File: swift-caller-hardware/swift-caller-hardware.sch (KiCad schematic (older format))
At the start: 3 parts

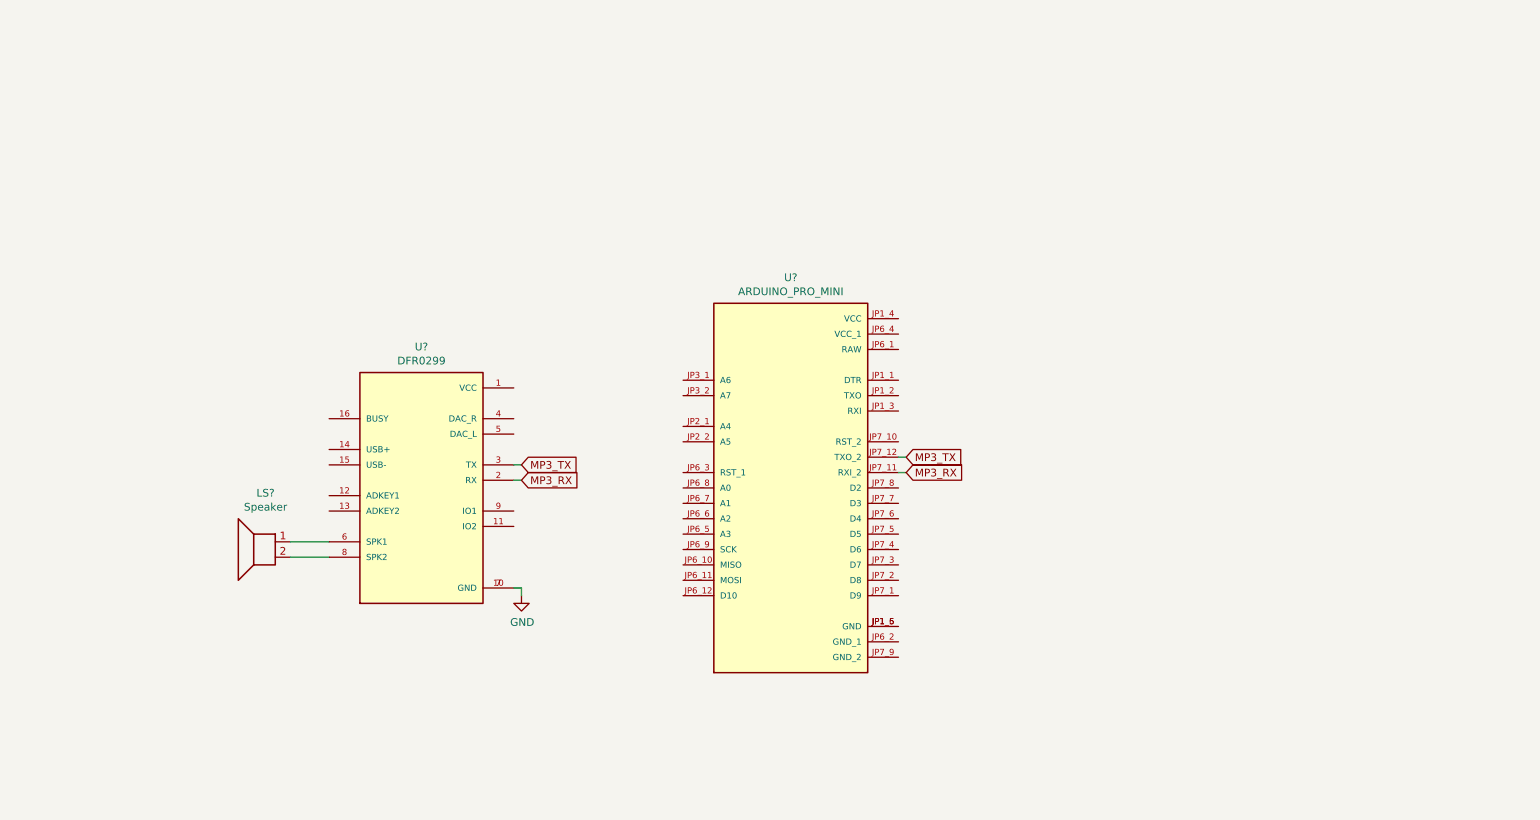
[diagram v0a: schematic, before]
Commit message: Update schematic and rename sub-directories
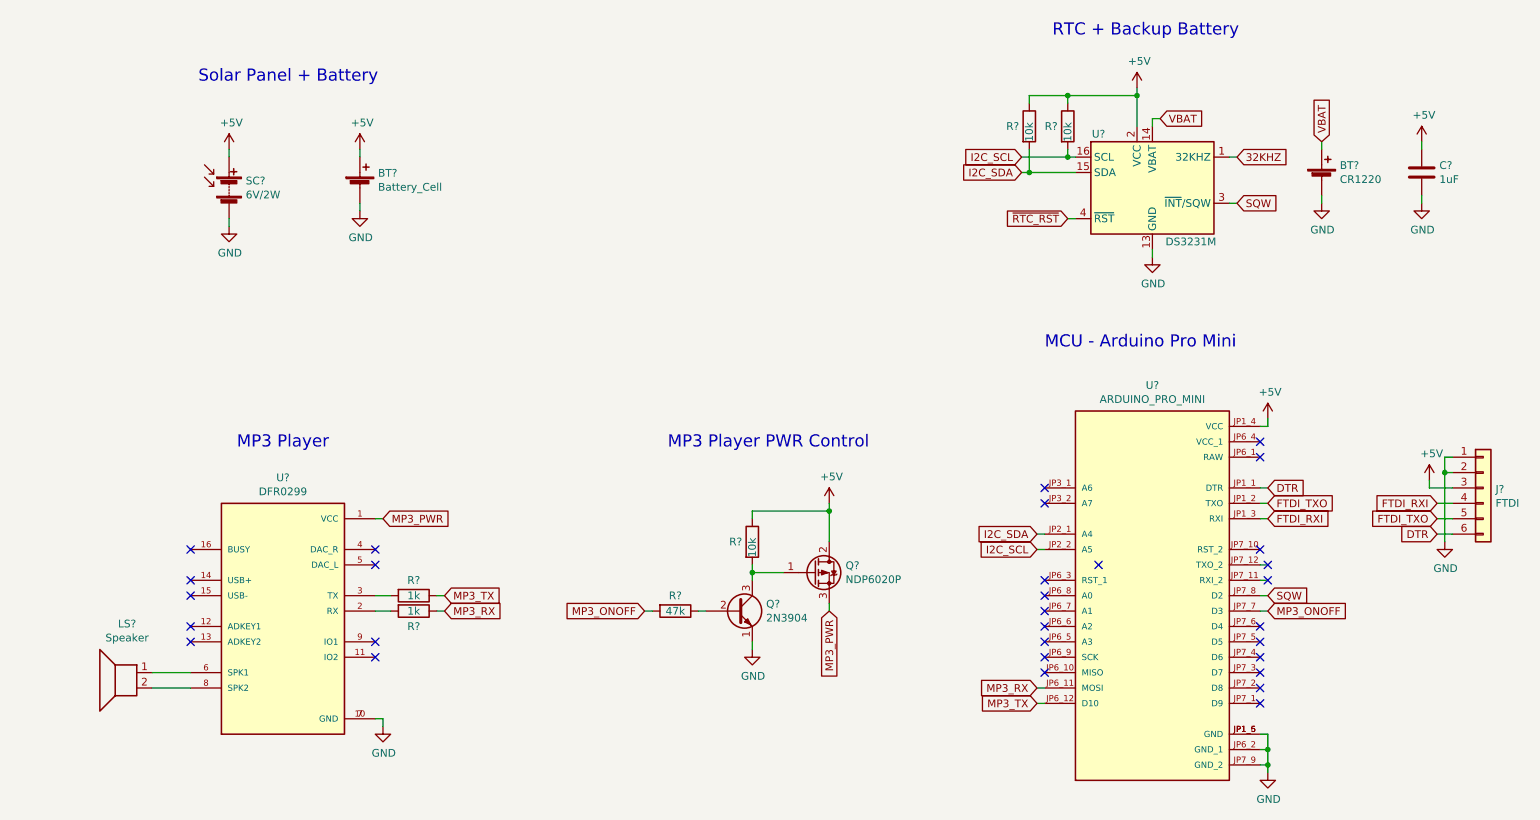
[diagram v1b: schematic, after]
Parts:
- added BT?: Battery_Cell, symbol Device:Battery_Cell
- added BT?: CR1220, symbol Device:Battery_Cell
- added C?: 1uF, symbol Device:C
- added J?: FTDI, symbol Connector_Generic:Conn_01x06
- added Q?: NDP6020P, symbol Device:Q_PMOS_GDS
- added Q?: 2N3904, Package_TO_SOT_THT:TO-92_Inline, symbol Transistor_BJT:2N3904
- added R? (x2): 1k, symbol Device:R
- added R? (x3): 10k, symbol Device:R
- added R?: 47k, symbol Device:R
- added SC?: 6V/2W, symbol Device:Solar_Cells
- added U?: DS3231M, Package_SO:SOIC-16W_7.5x10.3mm_P1.27mm, symbol Timer_RTC:DS3231M
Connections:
- net GND: now also U?.JP1_5 (GND), U?.JP1_6 (GND), U?.JP6_2 (GND_1), U?.JP7_9 (GND_2), BT?.2 (-), BT?.2 (-), C?.2, J?.1 (Pin_1), J?.2 (Pin_2), Q?.1 (E), SC?.2 (-), U?.10 (GND), U?.11 (GND), U?.12 (GND), U?.13 (GND), U?.5 (GND), U?.6 (GND), U?.7 (GND), U?.8 (GND), U?.9 (GND)
- net MP3_RX: now also U?.JP6_11 (MOSI), R?.1; no longer U?.2 (RX), U?.JP7_11 (RXI_2)
- net MP3_TX: now also U?.JP6_12 (D10), R?.1; no longer U?.3 (TX), U?.JP7_12 (TXO_2)
- net MP3_PWR: now reaches U?.1 (VCC)
- net MP3_PWR: now also Q?.3 (S)
- net DTR: now reaches U?.JP1_1 (DTR)
- net DTR: now also J?.6 (Pin_6)
- net FTDI_TXO: now reaches U?.JP1_2 (TXO)
- net FTDI_TXO: now also J?.5 (Pin_5)
- net FTDI_RXI: now reaches U?.JP1_3 (RXI)
- net FTDI_RXI: now also J?.4 (Pin_4)
- net +5V: now reaches U?.JP1_4 (VCC)
- net +5V: now also BT?.1 (+), C?.1, J?.3 (Pin_3), Q?.2 (D), R?.1, R?.1, R?.1, SC?.1 (+), U?.2 (VCC)
- net I2C_SDA: now reaches U?.JP2_1 (A4)
- net I2C_SDA: now also R?.2, U?.15 (SDA)
- net I2C_SCL: now reaches U?.JP2_2 (A5)
- net I2C_SCL: now also R?.2, U?.16 (SCL)
- net MP3_ONOFF: now reaches U?.JP7_7 (D3)
- net MP3_ONOFF: now also R?.2
- net SQW: now reaches U?.JP7_8 (D2)
- net SQW: now also U?.3 (~INT~/SQW)
- new net: R?.2, U?.2 (RX)
- new net: R?.2, U?.3 (TX)
- new net: Q?.1 (G), Q?.3 (C), R?.2
- new net: Q?.2 (B), R?.1
- new net 32KHZ: U?.1 (32KHZ)
- new net VBAT: BT?.1 (+), U?.14 (VBAT)
- new net ~RTC_RST: U?.4 (~RST)
- no-connect marks 0 -> 30
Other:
- note added: "MCU - Arduino Pro Mini\n"
- note added: "MP3 Player"
- note added: "MP3 Player PWR Control"
- note added: "RTC + Backup Battery\n\n"
- note added: "Solar Panel + Battery\n\n"
- moved on the sheet: LS?, U?

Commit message: Schematic and gitignore updates
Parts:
- R3: renamed from R?; value 47k -> 1k
- R4: renamed from R?; value 10k -> 1k
- gave numbers to parts that had none: 15
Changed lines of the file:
@@
 $EndDescr
 $Comp
-L ARDUINO_PRO_MINI:ARDUINO_PRO_MINI U?
+L ARDUINO_PRO_MINI:ARDUINO_PRO_MINI U3
 U 1 1 60281F94
 P 8450 4500
-F 0 "U?" H 8450 5867 50  0000 C CNN
+F 0 "U3" H 8450 5867 50  0000 C CNN
 F 1 "ARDUINO_PRO_MINI" H 8450 5776 50  0000 C CNN
 F 2 "MODULE_ARDUINO_PRO_MINI" H 8450 4500 50  0001 L BNN
@@
 	9150 4400 9200 4400
 $Comp
-L Device:Solar_Cells SC?
+L Device:Solar_Cells SC1
 U 1 1 6032913F
 P 2450 1850
-F 0 "SC?" H 2558 1896 50  0000 L CNN
+F 0 "SC1" H 2558 1896 50  0000 L CNN
 F 1 "6V/2W" H 2558 1805 50  0000 L CNN
 F 2 "" V 2450 1910 50  0001 C CNN
@@
 $EndComp
 $Comp
-L Device:Battery_Cell BT?
+L Device:Battery_Cell BT1
 U 1 1 60329DE0
 P 3300 1850
-F 0 "BT?" H 3418 1946 50  0000 L CNN
+F 0 "BT1" H 3418 1946 50  0000 L CNN
 F 1 "Battery_Cell" H 3418 1855 50  0000 L CNN
 F 2 "" V 3300 1910 50  0001 C CNN
@@
 $EndComp
 $Comp
-L power:+5V #PWR?
+L power:+5V #PWR03
 U 1 1 6032A68D
 P 3300 1600
-F 0 "#PWR?" H 3300 1450 50  0001 C CNN
+F 0 "#PWR03" H 3300 1450 50  0001 C CNN
 F 1 "+5V" H 3315 1773 50  0000 C CNN
 F 2 "" H 3300 1600 50  0001 C CNN
@@
 $EndComp
 $Comp
-L power:GND #PWR?
+L power:GND #PWR04
 U 1 1 6032AD07
 P 3300 2000
-F 0 "#PWR?" H 3300 1750 50  0001 C CNN
+F 0 "#PWR04" H 3300 1750 50  0001 C CNN
 F 1 "GND" H 3305 1827 50  0000 C CNN
 F 2 "" H 3300 2000 50  0001 C CNN
@@
 	3300 1650 3300 1600
 $Comp
-L power:+5V #PWR?
+L power:+5V #PWR010
 U 1 1 6032B549
 P 9200 3350
-F 0 "#PWR?" H 9200 3200 50  0001 C CNN
+F 0 "#PWR010" H 9200 3200 50  0001 C CNN
 F 1 "+5V" H 9215 3523 50  0000 C CNN
 F 2 "" H 9200 3350 50  0001 C CNN
@@
 	9200 3400 9200 3350
 $Comp
-L power:GND #PWR?
+L power:GND #PWR011
 U 1 1 6032BF3A
 P 9200 5650
-F 0 "#PWR?" H 9200 5400 50  0001 C CNN
+F 0 "#PWR011" H 9200 5400 50  0001 C CNN
 F 1 "GND" H 9205 5477 50  0000 C CNN
 F 2 "" H 9200 5650 50  0001 C CNN
@@
 	9200 5600 9200 5500
 $Comp
-L Timer_RTC:DS3231M U?
+L Timer_RTC:DS3231M U2
 U 1 1 6032D200
 P 8450 1850
-F 0 "U?" H 8100 2200 50  0000 C CNN
+F 0 "U2" H 8100 2200 50  0000 C CNN
 F 1 "DS3231M" H 8700 1500 50  0000 C CNN
 F 2 "Package_SO:SOIC-16W_7.5x10.3mm_P1.27mm" H 8450 1250 50  0001 C CNN
@@
 	8950 1950 9000 1950
 $Comp
-L power:+5V #PWR?
+L power:+5V #PWR08
 U 1 1 6032E32E
 P 8350 1200
-F 0 "#PWR?" H 8350 1050 50  0001 C CNN
+F 0 "#PWR08" H 8350 1050 50  0001 C CNN
 F 1 "+5V" H 8365 1373 50  0000 C CNN
 F 2 "" H 8350 1200 50  0001 C CNN
@@
 $EndComp
 $Comp
-L Device:Battery_Cell BT?
+L Device:Battery_Cell BT2
 U 1 1 6032EF52
 P 9550 1800
-F 0 "BT?" H 9668 1896 50  0000 L CNN
+F 0 "BT2" H 9668 1896 50  0000 L CNN
 F 1 "CR1220" H 9668 1805 50  0000 L CNN
 F 2 "" V 9550 1860 50  0001 C CNN
@@
 $EndComp
 $Comp
-L power:GND #PWR?
+L power:GND #PWR012
 U 1 1 6032FC0E
 P 9550 1950
-F 0 "#PWR?" H 9550 1700 50  0001 C CNN
+F 0 "#PWR012" H 9550 1700 50  0001 C CNN
 F 1 "GND" H 9555 1777 50  0000 C CNN
 F 2 "" H 9550 1950 50  0001 C CNN
@@
 	9550 1950 9550 1900
 $Comp
-L power:GND #PWR?
+L power:GND #PWR09
 U 1 1 60330710
 P 8450 2300
-F 0 "#PWR?" H 8450 2050 50  0001 C CNN
+F 0 "#PWR09" H 8450 2050 50  0001 C CNN
 F 1 "GND" H 8455 2127 50  0000 C CNN
 F 2 "" H 8450 2300 50  0001 C CNN
@@
 	7900 2050 7950 2050
 $Comp
-L Device:R R?
+L Device:R R6
 U 1 1 60333669
 P 7900 1450
-F 0 "R?" H 7750 1450 50  0000 L CNN
+F 0 "R6" H 7750 1450 50  0000 L CNN
 F 1 "10k" V 7900 1350 50  0000 L CNN
 F 2 "" V 7830 1450 50  0001 C CNN
@@
 Connection ~ 8350 1250
 $Comp
-L Device:C C?
+L Device:C C1
 U 1 1 60337929
 P 10200 1750
-F 0 "C?" H 10315 1796 50  0000 L CNN
+F 0 "C1" H 10315 1796 50  0000 L CNN
 F 1 "1uF" H 10315 1705 50  0000 L CNN
 F 2 "" H 10238 1600 50  0001 C CNN
@@
 $EndComp
 $Comp
-L power:GND #PWR?
+L power:GND #PWR014
 U 1 1 60337D95
 P 10200 1950
-F 0 "#PWR?" H 10200 1700 50  0001 C CNN
+F 0 "#PWR014" H 10200 1700 50  0001 C CNN
 F 1 "GND" H 10205 1777 50  0000 C CNN
 F 2 "" H 10200 1950 50  0001 C CNN
@@
 	10200 1950 10200 1900
 $Comp
-L power:+5V #PWR?
+L power:+5V #PWR013
 U 1 1 603386A2
 P 10200 1550
-F 0 "#PWR?" H 10200 1400 50  0001 C CNN
+F 0 "#PWR013" H 10200 1400 50  0001 C CNN
 F 1 "+5V" H 10215 1723 50  0000 C CNN
 F 2 "" H 10200 1550 50  0001 C CNN
@@
 	9200 4600 9150 4600
 $Comp
-L power:+5V #PWR?
+L power:+5V #PWR01
 U 1 1 6033B76D
 P 2450 1600
-F 0 "#PWR?" H 2450 1450 50  0001 C CNN
+F 0 "#PWR01" H 2450 1450 50  0001 C CNN
 F 1 "+5V" H 2465 1773 50  0000 C CNN
 F 2 "" H 2450 1600 50  0001 C CNN
@@
 	2450 1600 2450 1650
 $Comp
-L power:GND #PWR?
+L power:GND #PWR02
 U 1 1 6033C4C8
 P 2450 2100
-F 0 "#PWR?" H 2450 1850 50  0001 C CNN
+F 0 "#PWR02" H 2450 1850 50  0001 C CNN
 F 1 "GND" H 2455 1927 50  0000 C CNN
 F 2 "" H 2450 2100 50  0001 C CNN
@@
 NoConn ~ 9150 3500
 $Comp
-L Device:Q_PMOS_GDS Q?
+L Device:Q_PMOS_GDS Q2
 U 1 1 60340ED9
 P 6250 4350
-F 0 "Q?" H 6456 4396 50  0000 L CNN
+F 0 "Q2" H 6456 4396 50  0000 L CNN
 F 1 "NDP6020P" H 6456 4305 50  0000 L CNN
 F 2 "" H 6450 4450 50  0001 C CNN
@@
 $EndComp
 $Comp
-L power:+5V #PWR?
+L power:+5V #PWR07
 U 1 1 60341438
 P 6350 3900
-F 0 "#PWR?" H 6350 3750 50  0001 C CNN
+F 0 "#PWR07" H 6350 3750 50  0001 C CNN
 F 1 "+5V" H 6365 4073 50  0000 C CNN
 F 2 "" H 6350 3900 50  0001 C CNN
@@
 	6350 4600 6350 4550
 $Comp
-L Transistor_BJT:2N3904 Q?
+L Transistor_BJT:2N3904 Q1
 U 1 1 603431EA
 P 5750 4600
-F 0 "Q?" H 5940 4646 50  0000 L CNN
+F 0 "Q1" H 5940 4646 50  0000 L CNN
 F 1 "2N3904" H 5940 4555 50  0000 L CNN
 F 2 "Package_TO_SOT_THT:TO-92_Inline" H 5950 4525 50  0001 L CIN
@@
 $EndComp
 $Comp
-L Device:R R?
+L Device:R R4
 U 1 1 603441EB
 P 5850 4150
-F 0 "R?" H 5700 4150 50  0000 L CNN
-F 1 "10k" V 5850 4050 50  0000 L CNN
+F 0 "R4" H 5700 4150 50  0000 L CNN
+F 1 "1k" V 5850 4100 50  0000 L CNN
 F 2 "" V 5780 4150 50  0001 C CNN
 F 3 "~" H 5850 4150 50  0001 C CNN
@@
 	6350 3900 6350 3950
 $Comp
-L power:GND #PWR?
+L power:GND #PWR06
 U 1 1 60349585
 P 5850 4850
-F 0 "#PWR?" H 5850 4600 50  0001 C CNN
+F 0 "#PWR06" H 5850 4600 50  0001 C CNN
 F 1 "GND" H 5855 4677 50  0000 C CNN
 F 2 "" H 5850 4850 50  0001 C CNN
@@
 MP3_ONOFF
 $Comp
-L Device:R R?
+L Device:R R3
 U 1 1 6036406F
 P 5350 4600
-F 0 "R?" V 5250 4600 50  0000 C CNN
-F 1 "47k" V 5350 4600 50  0000 C CNN
+F 0 "R3" V 5250 4600 50  0000 C CNN
+F 1 "1k" V 5350 4600 50  0000 C CNN
 F 2 "" V 5280 4600 50  0001 C CNN
 F 3 "~" H 5350 4600 50  0001 C CNN
@@
 	7650 1300 7650 1250
 $Comp
-L Device:R R?
+L Device:R R5
 U 1 1 60333D10
 P 7650 1450
-F 0 "R?" H 7500 1450 50  0000 L CNN
+F 0 "R5" H 7500 1450 50  0000 L CNN
 F 1 "10k" V 7650 1350 50  0000 L CNN
 F 2 "" V 7580 1450 50  0001 C CNN
@@
 	9150 4000 9200 4000
 $Comp
-L Connector_Generic:Conn_01x06 J?
+L Connector_Generic:Conn_01x06 J1
 U 1 1 603BCDB1
 P 10600 3800
-F 0 "J?" H 10680 3792 50  0000 L CNN
+F 0 "J1" H 10680 3792 50  0000 L CNN
 F 1 "FTDI" H 10680 3701 50  0000 L CNN
 F 2 "" H 10600 3800 50  0001 C CNN
@@
 $EndComp
 $Comp
-L power:GND #PWR?
+L power:GND #PWR016
 U 1 1 603BDF8D
 P 10350 4150
-F 0 "#PWR?" H 10350 3900 50  0001 C CNN
+F 0 "#PWR016" H 10350 3900 50  0001 C CNN
 F 1 "GND" H 10355 3977 50  0000 C CNN
 F 2 "" H 10350 4150 50  0001 C CNN
@@
 	10350 3700 10350 3600
 $Comp
-L power:+5V #PWR?
+L power:+5V #PWR015
 U 1 1 603C0DE3
 P 10250 3750
-F 0 "#PWR?" H 10250 3600 50  0001 C CNN
+F 0 "#PWR015" H 10250 3600 50  0001 C CNN
 F 1 "+5V" H 10265 3923 50  0000 C CNN
 F 2 "" H 10250 3750 50  0001 C CNN
@@
 	3800 4600 3850 4600
 $Comp
-L Device:R R?
+L Device:R R2
 U 1 1 603267E2
 P 3650 4600
-F 0 "R?" V 3750 4600 50  0000 C CNN
+F 0 "R2" V 3750 4600 50  0000 C CNN
 F 1 "1k" V 3650 4600 50  0000 C CNN
 F 2 "" V 3580 4600 50  0001 C CNN
@@
 	3400 4500 3500 4500
 $Comp
-L Device:R R?
+L Device:R R1
 U 1 1 60325C5E
 P 3650 4500
-F 0 "R?" V 3550 4500 50  0000 C CNN
+F 0 "R1" V 3550 4500 50  0000 C CNN
 F 1 "1k" V 3650 4500 50  0000 C CNN
 F 2 "" V 3580 4500 50  0001 C CNN
@@
 	3450 5350 3450 5300
 $Comp
-L power:GND #PWR?
+L power:GND #PWR05
 U 1 1 60283CBF
 P 3450 5350
-F 0 "#PWR?" H 3450 5100 50  0001 C CNN
+F 0 "#PWR05" H 3450 5100 50  0001 C CNN
 F 1 "GND" H 3455 5177 50  0000 C CNN
 F 2 "" H 3450 5350 50  0001 C CNN
@@
 	1950 5000 2200 5000
 $Comp
-L DFR0299:DFR0299 U?
+L DFR0299:DFR0299 U1
 U 1 1 6027F757
 P 2800 4600
-F 0 "U?" H 2800 5467 50  0000 C CNN
+F 0 "U1" H 2800 5467 50  0000 C CNN
 F 1 "DFR0299" H 2800 5376 50  0000 C CNN
 F 2 "MODULE_DFR0299" H 2800 4600 50  0001 L BNN
@@
 $EndComp
 $Comp
-L Device:Speaker LS?
+L Device:Speaker LS1
 U 1 1 6027F053
 P 1750 5000
-F 0 "LS?" H 1713 5317 50  0000 C CNN
+F 0 "LS1" H 1713 5317 50  0000 C CNN
 F 1 "Speaker" H 1713 5226 50  0000 C CNN
 F 2 "" H 1750 4800 50  0001 C CNN

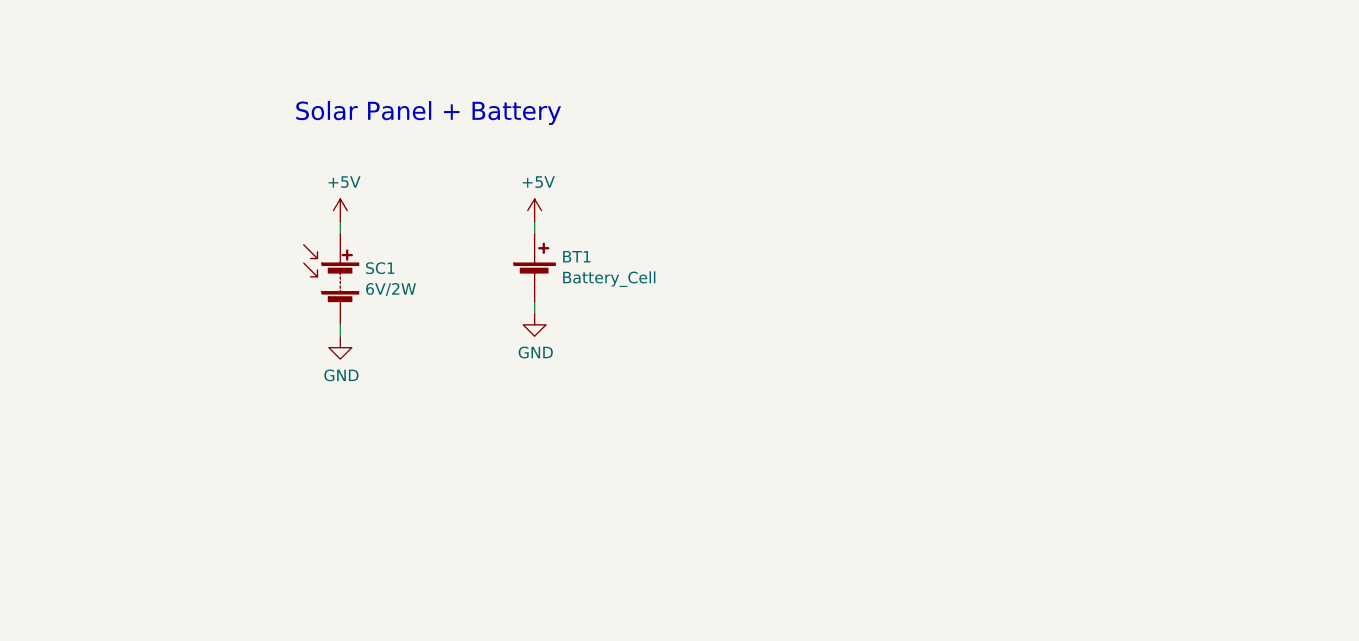
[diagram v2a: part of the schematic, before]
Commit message: Update solar panel, charger and battery circuit
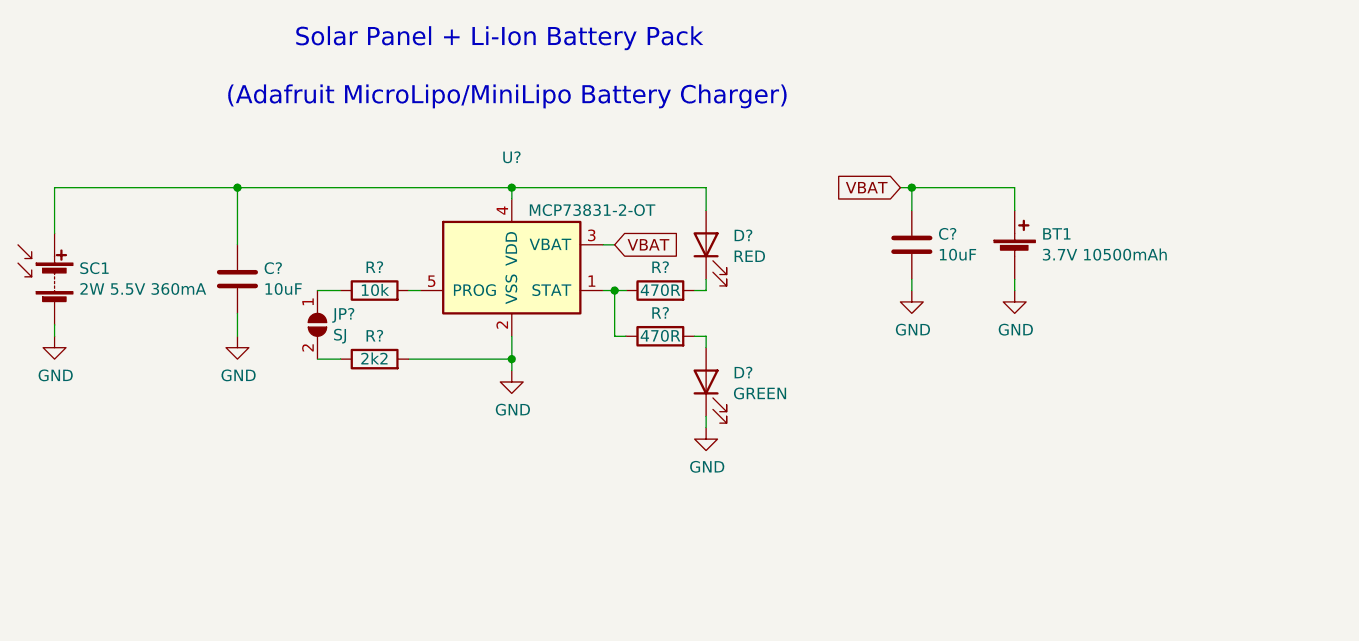
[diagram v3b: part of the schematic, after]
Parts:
- added C? (x2): 10uF, symbol Device:C
- added D?: RED, symbol Device:LED
- added D?: GREEN, symbol Device:LED
- added JP?: SJ, symbol Jumper:SolderJumper_2_Open
- added R? (x2): 470R, symbol Device:R
- added R?: 10k, symbol Device:R
- added R?: 2k2, symbol Device:R
- added U?: MCP73831-2-OT, Package_TO_SOT_SMD:SOT-23-5, symbol Battery_Management:MCP73831-2-OT
- BT1: value Battery_Cell -> 3.7V 10500mAh
- SC1: value 6V/2W -> 2W 5.5V 360mA
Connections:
- net +5V: no longer BT1.1 (+), SC1.1 (+)
- net GND: now also C?.2, C?.2, D?.1 (K), R?.2, U?.2 (VSS)
- net VBAT: now also BT1.1 (+), C?.1, U?.3 (VBAT)
- new net: C?.1, D?.2 (A), SC1.1 (+), U?.4 (VDD)
- new net: R?.1, R?.1, U?.1 (STAT)
- new net: R?.2, U?.5 (PROG)
- new net: D?.1 (K), R?.2
- new net: D?.2 (A), R?.2
- new net: JP?.1 (A), R?.1
- new net: JP?.2 (B), R?.1
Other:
- note added: "(Adafruit MicroLipo/MiniLipo Battery Charger)"
- note added: "Solar Panel + Li-Ion Battery Pack\n\n\n"
- note removed: "Solar Panel + Battery\n\n"
- moved on the sheet: BT1, SC1
